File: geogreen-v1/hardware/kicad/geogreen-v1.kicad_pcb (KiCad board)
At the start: 2 copper layers, 85 x 57 mm, 29 parts, among them J1 USB-C, J2 IP67_SENSOR_CANDIDATE, J3 A02YYUW_4WIRE, J4 RGB_SEMAFORO, U1 ESP32-C6-MINI-1, U2 3V3_REG_TODO

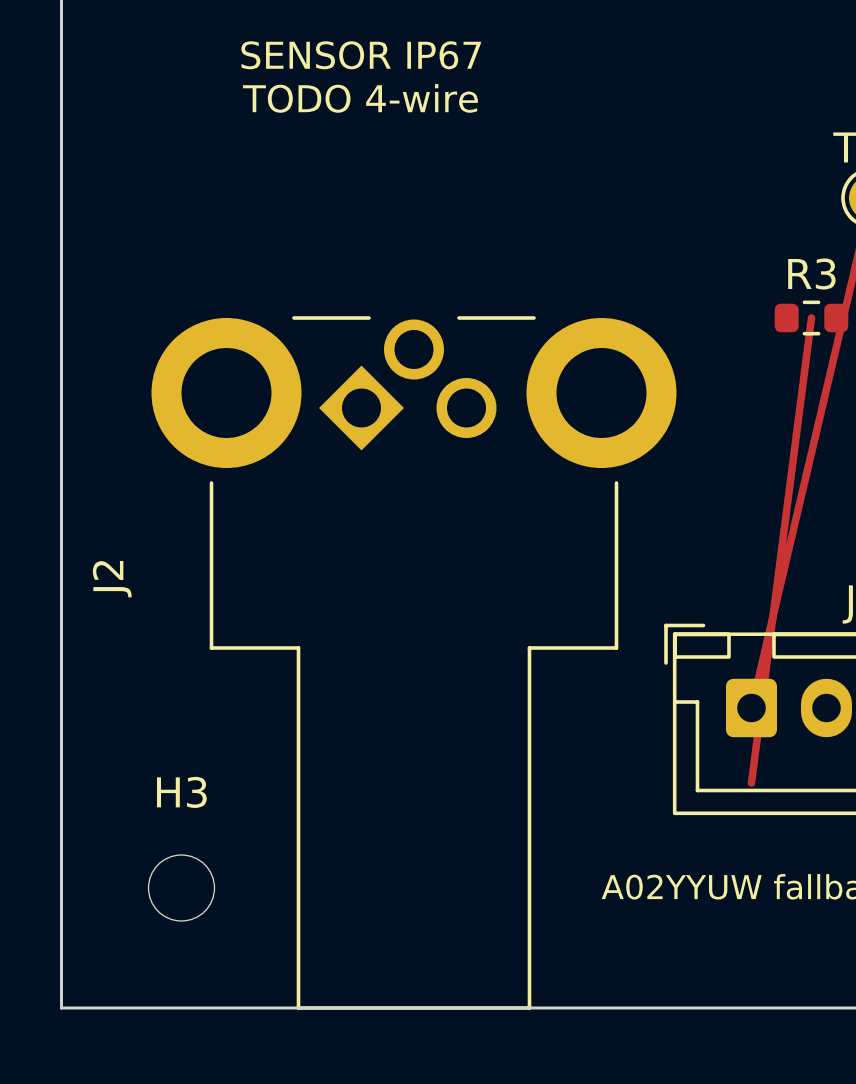
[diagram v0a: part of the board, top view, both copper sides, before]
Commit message: add V1 mechanical STEP models
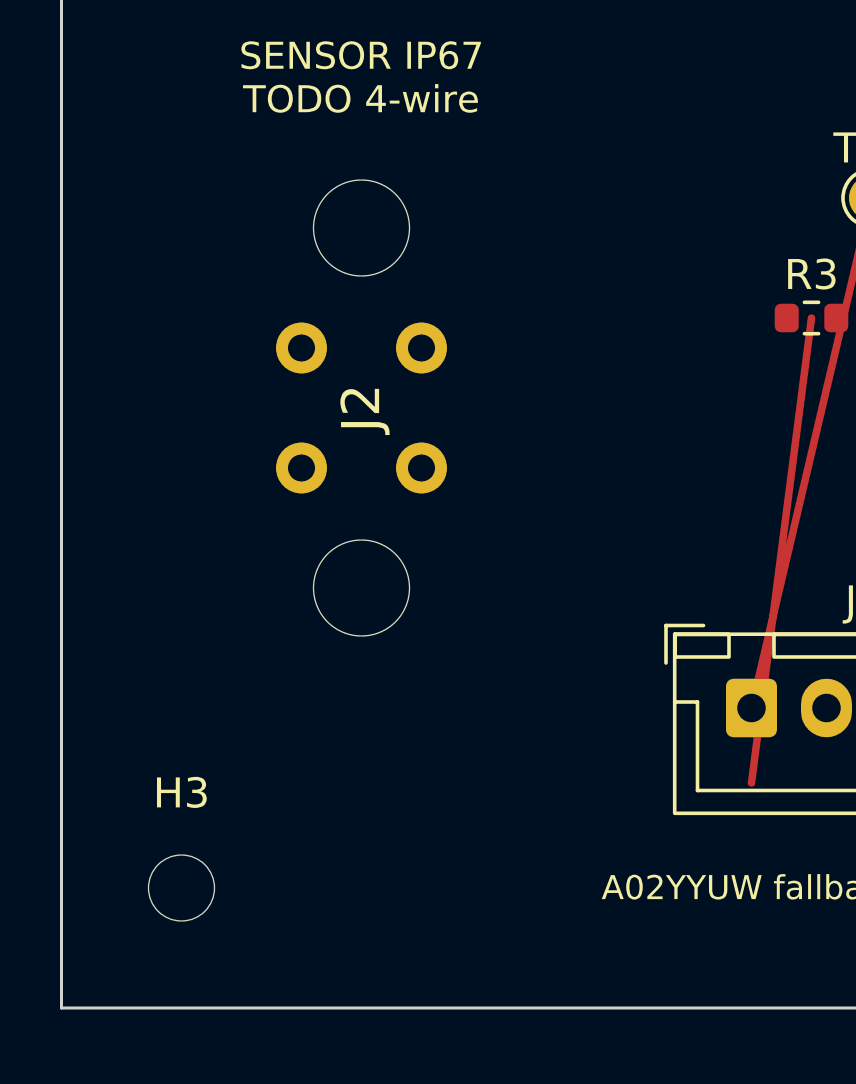
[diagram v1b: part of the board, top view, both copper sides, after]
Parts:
- J2: value IP67_SENSOR_CANDIDATE -> M8_4PIN_IP67_SENSOR; footprint Amphenol_M8S-03PMMR-SF8001 -> (none)
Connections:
- J2 pad 1: (no net) -> 3V3
- J2 pad 2: (no net) -> GND
- J2 pad 3: (no net) -> SENSOR_UART_RX

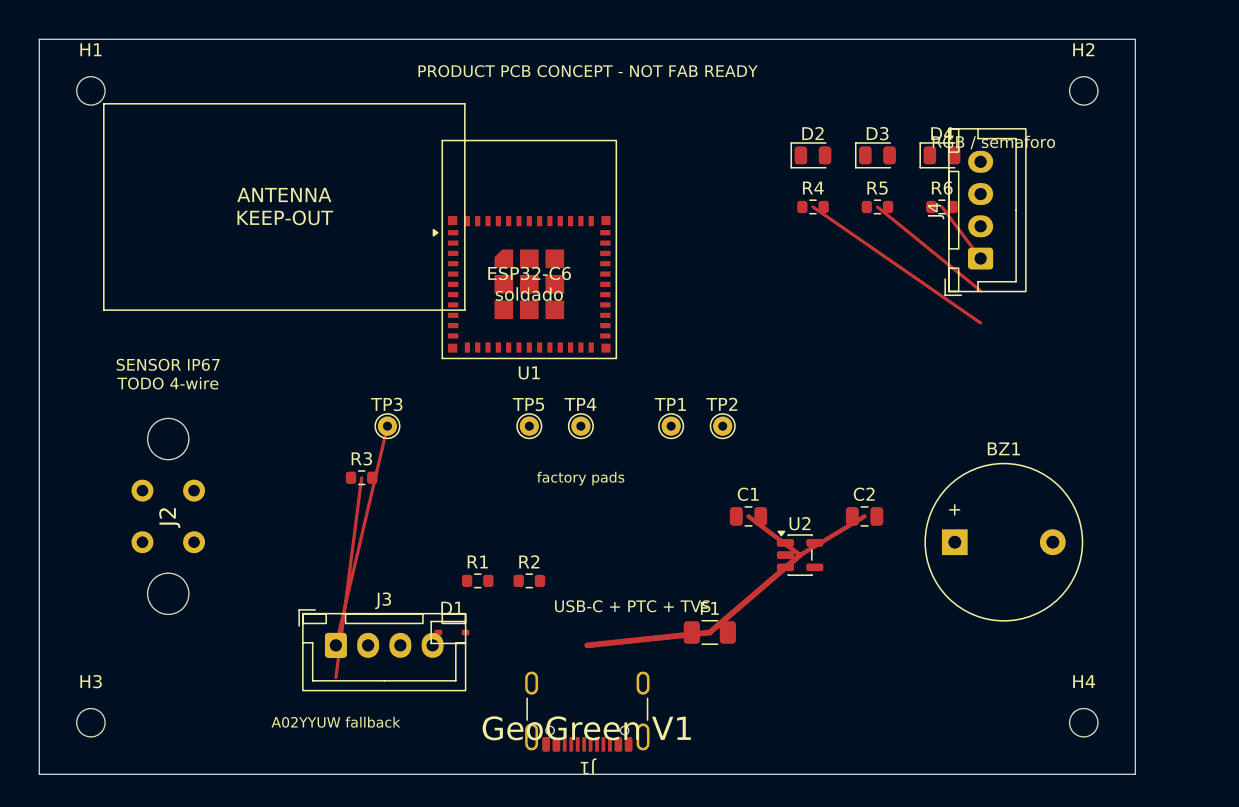
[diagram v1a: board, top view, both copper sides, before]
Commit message: make GeoGreen V1 PCB fabrication candidate
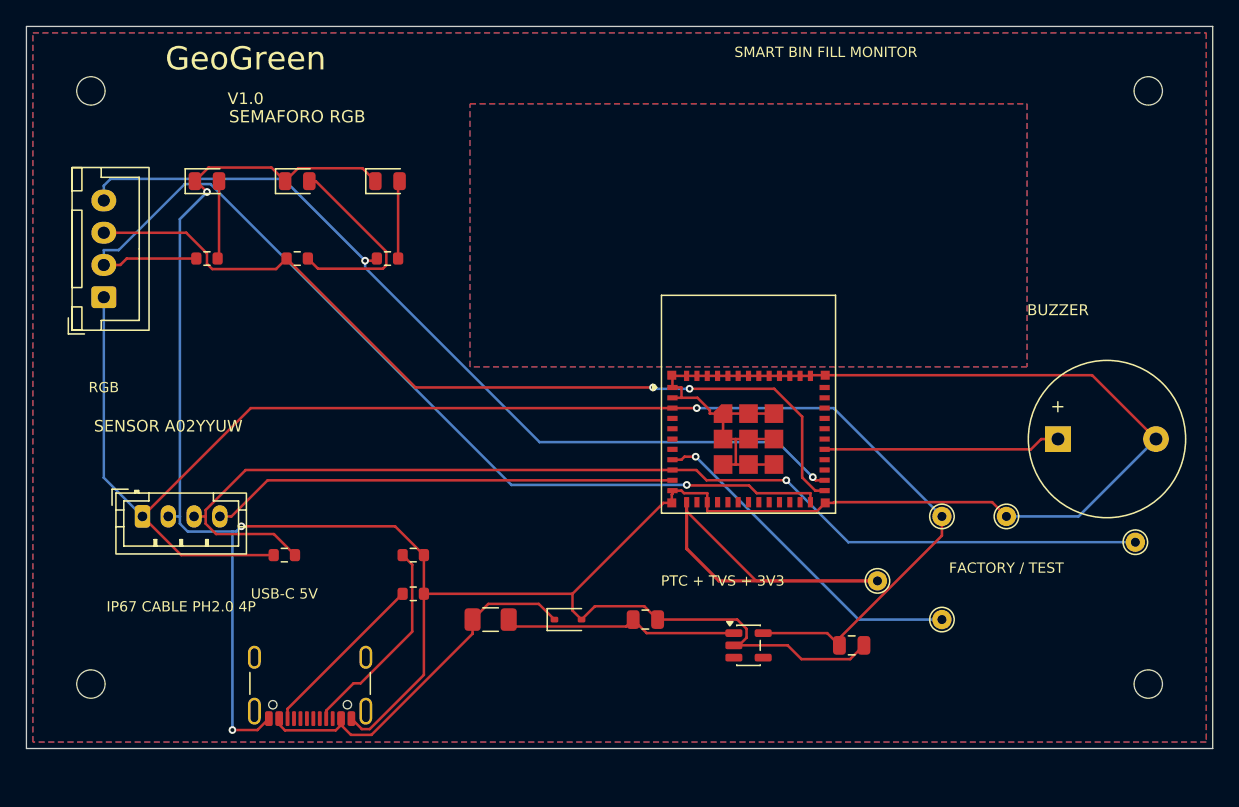
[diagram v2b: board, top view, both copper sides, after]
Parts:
- removed J3: A02YYUW_4WIRE, JST_XH_B4B-XH-A_1x04_P2.50mm_Vertical
- D1: value TVS_USB -> TVS
- F1: value PTC_USB -> PTC
- J2: value M8_4PIN_IP67_SENSOR -> A02YYUW_PH2.0; footprint (none) -> JST_PH_B4B-PH-K_1x04_P2.00mm_Vertical
- R4: value LED_R_LIMIT -> LED_R_1K
- R5: value LED_G_LIMIT -> LED_G_1K
- R6: value LED_B_LIMIT -> LED_B_1K
- U2: value 3V3_REG_TODO -> 3V3_REG
- moved J4 68.1 mm to (10.0, 25.0)
- moved TP3 58.7 mm to (90.0, 44.0)
- moved R4 47.2 mm to (18.0, 22.0)
- moved D2 47.0 mm to (18.0, 16.0)
- moved R5 45.2 mm to (25.0, 22.0)
- moved D3 45.0 mm to (25.0, 16.0)
- moved R6 43.2 mm to (32.0, 22.0)
- moved D4 43.0 mm to (32.0, 16.0)
- moved TP4 31.8 mm to (75.0, 50.0)
- moved TP5 29.5 mm to (70.0, 47.0)
- moved TP2 23.1 mm to (80.0, 42.0)
- moved TP1 22.1 mm to (75.0, 42.0)
- moved J1 21.6 mm to (26.0, 54.0)
- moved U1 20.8 mm to (60.0, 36.0)
- moved F1 17.0 mm to (40.0, 50.0)
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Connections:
- D1 pad 1: (no net) -> VBUS_USB
- D1 pad 2: (no net) -> GND
- D2 pad 1: (no net) -> GND
- D2 pad 2: (no net) -> LED_R_ANODE
- D3 pad 1: (no net) -> GND
- D3 pad 2: (no net) -> LED_G_ANODE
- D4 pad 1: (no net) -> GND
- D4 pad 2: (no net) -> LED_B_ANODE
- J1 pad A5: (no net) -> USB_CC1
- J1 pad B5: (no net) -> USB_CC2
- R1 pad 1: (no net) -> USB_CC1
- R1 pad 2: (no net) -> GND
- R2 pad 1: (no net) -> USB_CC2
- R2 pad 2: (no net) -> GND
- R3 pad 1: (no net) -> 3V3
- R3 pad 2: (no net) -> SENSOR_UART_RX
- R4 pad 1: (no net) -> LED_R
- R4 pad 2: (no net) -> LED_R_ANODE
- R5 pad 1: (no net) -> LED_G
- R5 pad 2: (no net) -> LED_G_ANODE
- R6 pad 1: (no net) -> LED_B
- R6 pad 2: (no net) -> LED_B_ANODE
- TP1 pad 1: (no net) -> 3V3
- TP2 pad 1: (no net) -> GND
- TP3 pad 1: (no net) -> SENSOR_UART_RX
- TP4 pad 1: (no net) -> EN
- TP5 pad 1: (no net) -> BOOT_IO0
- U1 pad 1: (no net) -> GND
- U1 pad 10: (no net) -> SENSOR_RX_PULLUP
- U1 pad 11: (no net) -> GND
- U1 pad 12: (no net) -> BOOT_IO0
- U1 pad 14: (no net) -> GND
- U1 pad 2: (no net) -> GND
- U1 pad 24: (no net) -> LED_R
- U1 pad 25: (no net) -> LED_G
- U1 pad 26: (no net) -> LED_B
- U1 pad 29: (no net) -> BUZZER_OUT
- U1 pad 3: (no net) -> 3V3
- U1 pad 36: (no net) -> GND
- U1 pad 37: (no net) -> GND
- U1 pad 38: (no net) -> GND
- U1 pad 39: (no net) -> GND
- U1 pad 40: (no net) -> GND
- U1 pad 41: (no net) -> GND
- U1 pad 42: (no net) -> GND
- U1 pad 43: (no net) -> GND
- U1 pad 44: (no net) -> GND
- U1 pad 45: (no net) -> GND
- U1 pad 46: (no net) -> GND
- U1 pad 47: (no net) -> GND
- U1 pad 48: (no net) -> GND
- U1 pad 49: (no net) -> GND
- U1 pad 50: (no net) -> GND
- U1 pad 51: (no net) -> GND
- U1 pad 52: (no net) -> GND
- U1 pad 53: (no net) -> GND
- U1 pad 8: (no net) -> EN
- U1 pad 9: (no net) -> SENSOR_UART_RX
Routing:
- net GND: track 0.00 -> 257.2 mm, vias 0 -> 3
- net SENSOR_UART_RX: track 0.00 -> 85.6 mm, vias 0 -> 1
- net 3V3: track 43.9 -> 118.1 mm, vias 0 -> 1
- net LED_B: track 0.00 -> 68.3 mm, vias 0 -> 2
- net LED_R: track 15.8 -> 76.1 mm, vias 0 -> 1
- net LED_G: track 10.3 -> 68.1 mm, vias 0 -> 2
- net BOOT_IO0: track 0.00 -> 37.2 mm
- net SENSOR_RX_PULLUP: track 0.00 -> 36.3 mm
- net EN: track 0.00 -> 26.2 mm, vias 0 -> 1
- net VBUS_USB: track 9.55 -> 28.3 mm
- net BUZZER_OUT: track 0.00 -> 18.4 mm
- net USB_CC1: track 0.00 -> 16.1 mm
- net LED_G_ANODE: track 0.00 -> 15.8 mm
- net USB_CC2: track 0.00 -> 13.4 mm
- net LED_R_ANODE: track 0.00 -> 6.05 mm
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- added copper zone on B.Cu, net GND
- added copper zone on F.Cu, net GND
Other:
- board size 85 x 57 mm -> 92 x 56 mm
- board text added: "BUZZER"
- board text added: "CC 5K1"
- board text added: "ESP32-C6-MINI-1"
- board text added: "FACTORY / TEST"
- board text added: "GeoGreen"
- board text added: "IP67 CABLE PH2.0 4P"
- board text added: "PTC + TVS + 3V3"
- board text added: "RGB"
- board text added: "SEMAFORO RGB"
- board text added: "SENSOR A02YYUW"
- board text added: "SMART BIN FILL MONITOR"
- board text added: "USB-C 5V"
- board text added: "V1.0"
- board text removed: "A02YYUW fallback"
- board text removed: "ESP32-C6 soldado"
- board text removed: "GeoGreen V1"
- board text removed: "PRODUCT PCB CONCEPT - NOT FAB READY"
- board text removed: "RGB / semaforo"
- board text removed: "SENSOR IP67 TODO 4-wire"
- board text removed: "USB-C + PTC + TVS"
- board text removed: "factory pads"
